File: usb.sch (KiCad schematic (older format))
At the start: 27 parts, among them IC1 EP4CE10F17, P1 USB_A, U23 FT313HL-LQFP64-0.5, U25 TPS2024D, Y2 Geyer_KX7_12MHz

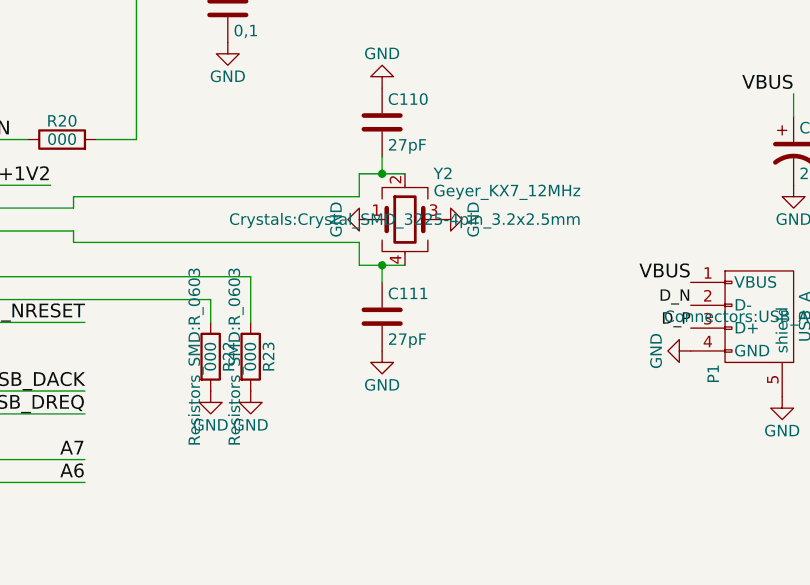
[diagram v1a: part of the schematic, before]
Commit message: Crystals fix, USB rearranged
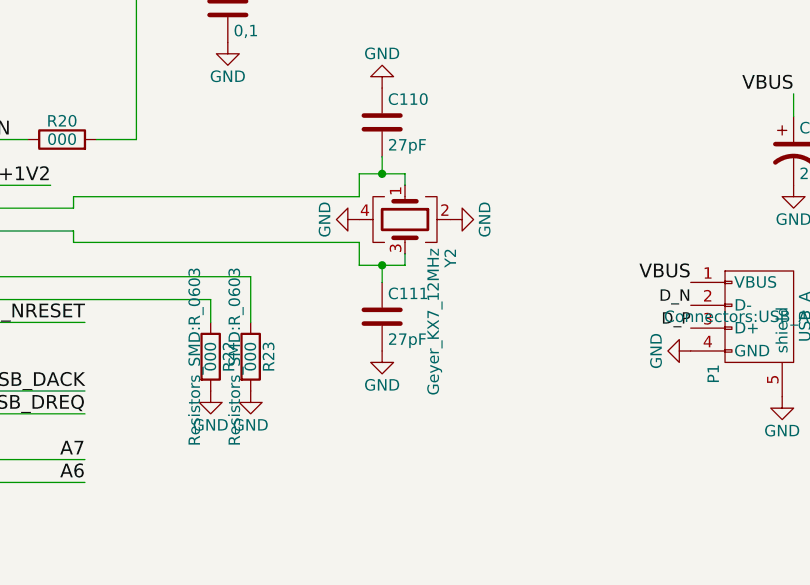
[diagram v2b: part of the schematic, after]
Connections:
- net GND: now also Y2.2, Y2.4; no longer Y2.1, Y2.3
- net at C111.1, U23.44 (X1/CLKIN): now also Y2.3; no longer Y2.4
- net at C110.2, U23.45 (X2): now also Y2.1; no longer Y2.2
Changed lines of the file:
@@
 F 0 "Y2" H 9075 3475 50  0000 L CNN
 F 1 "Geyer_KX7_12MHz" H 9075 3400 50  0000 L CNN
-F 2 "Crystals:Crystal_SMD_3225-4pin_3.2x2.5mm" H 8950 3275 50  0000 C CNN
+F 2 "Crystals:Crystal_SMD_3225-4pin_3.2x2.5mm" H 8950 3275 50  0001 C CNN
 F 3 "" H 8950 3275 50  0000 C CNN
 	1    8950 3275
-	1    0    0    -1
+	0    1    1    0
 $EndComp
 Wire Wire Line
@@
 L GND #PWR0164
 U 1 1 5891C617
-P 8800 3275
-F 0 "#PWR0164" H 8800 3025 50  0001 C CNN
-F 1 "GND" H 8800 3125 50  0000 C CNN
-F 2 "" H 8800 3275 50  0000 C CNN
-F 3 "" H 8800 3275 50  0000 C CNN
-	1    8800 3275
+P 8750 3275
+F 0 "#PWR0164" H 8750 3025 50  0001 C CNN
+F 1 "GND" H 8750 3125 50  0000 C CNN
+F 2 "" H 8750 3275 50  0000 C CNN
+F 3 "" H 8750 3275 50  0000 C CNN
+	1    8750 3275
 	0    1    1    0
 $EndComp
@@
 L GND #PWR0165
 U 1 1 5891C65E
-P 9100 3275
-F 0 "#PWR0165" H 9100 3025 50  0001 C CNN
-F 1 "GND" H 9100 3125 50  0000 C CNN
-F 2 "" H 9100 3275 50  0000 C CNN
-F 3 "" H 9100 3275 50  0000 C CNN
-	1    9100 3275
+P 9150 3275
+F 0 "#PWR0165" H 9150 3025 50  0001 C CNN
+F 1 "GND" H 9150 3125 50  0000 C CNN
+F 2 "" H 9150 3275 50  0000 C CNN
+F 3 "" H 9150 3275 50  0000 C CNN
+	1    9150 3275
 	0    -1   -1   0
 $EndComp
@@
 Text GLabel 5125 5100 3    39   Input ~ 0
 ETHSD15
+Wire Wire Line
+	8950 3075 8950 3125
+Wire Wire Line
+	8950 3475 8950 3425
 $EndSCHEMATC

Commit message: Added VBUS and OC LEDs
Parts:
- added D1: RED, LEDs:LED_0603, symbol LED_Small_ALT
- added D2: GREEN, LEDs:LED_0603, symbol LED_Small_ALT
- added R26, R27: TBD, Resistors_SMD:R_0603, symbol R
- Y2: value Geyer_KX7_12MHz -> 12MHz
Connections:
- net +3V3: now also R26.1
- net GND: now also R27.2
- net VBUS: now also D2.2 (A)
- net at R24.2, R25.1, U25.5 (~OC): now also D1.1 (K)
- new net: D2.1 (K), R27.1
- new net: D1.2 (A), R26.2
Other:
- moved on the sheet: C108, C109, C65, C66, C67, C68, C69, C70, R25

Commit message: Add CPEx config resistors
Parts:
- added R28, R29: 000, Resistors_SMD:R_0603, symbol R
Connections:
- net CPE0: now also R28.2
- net CPE1: now also R29.2
- net GND: now also R28.1, R29.1
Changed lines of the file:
@@
 $EndComp
 $Comp
-L GND #PWR151
+L GND #PWR153
 U 1 1 587F942A
 P 7000 3425
-F 0 "#PWR151" H 7000 3175 50  0001 C CNN
+F 0 "#PWR153" H 7000 3175 50  0001 C CNN
 F 1 "GND" H 7000 3275 50  0000 C CNN
 F 2 "" H 7000 3425 50  0000 C CNN
@@
 $EndComp
 $Comp
-L GND #PWR150
+L GND #PWR152
 U 1 1 587F944F
 P 7000 3025
-F 0 "#PWR150" H 7000 2775 50  0001 C CNN
+F 0 "#PWR152" H 7000 2775 50  0001 C CNN
 F 1 "GND" H 7000 2875 50  0000 C CNN
 F 2 "" H 7000 3025 50  0000 C CNN
@@
 $EndComp
 $Comp
-L GND #PWR147
+L GND #PWR149
 U 1 1 587F9489
 P 5825 2450
-F 0 "#PWR147" H 5825 2200 50  0001 C CNN
+F 0 "#PWR149" H 5825 2200 50  0001 C CNN
 F 1 "GND" H 5825 2300 50  0000 C CNN
 F 2 "" H 5825 2450 50  0000 C CNN
@@
 $EndComp
 $Comp
-L GND #PWR144
+L GND #PWR146
 U 1 1 587F9497
 P 5425 2450
-F 0 "#PWR144" H 5425 2200 50  0001 C CNN
+F 0 "#PWR146" H 5425 2200 50  0001 C CNN
 F 1 "GND" H 5425 2300 50  0000 C CNN
 F 2 "" H 5425 2450 50  0000 C CNN
@@
 $EndComp
 $Comp
-L +3V3 #PWR165
+L +3V3 #PWR167
 U 1 1 587FA4A0
 P 10075 675
-F 0 "#PWR165" H 10175 725 20  0001 C CNN
+F 0 "#PWR167" H 10175 725 20  0001 C CNN
 F 1 "+3V3" H 10075 765 30  0000 C CNN
 F 2 "" H 10075 675 60  0000 C CNN
@@
 $EndComp
 $Comp
-L GND #PWR166
+L GND #PWR168
 U 1 1 587FA6CC
 P 10075 1075
-F 0 "#PWR166" H 10075 825 50  0001 C CNN
+F 0 "#PWR168" H 10075 825 50  0001 C CNN
 F 1 "GND" H 10075 925 50  0000 C CNN
 F 2 "" H 10075 1075 50  0000 C CNN
@@
 $EndComp
 $Comp
-L +3V3 #PWR146
+L +3V3 #PWR148
 U 1 1 587FB177
 P 5725 5100
-F 0 "#PWR146" H 5825 5150 20  0001 C CNN
+F 0 "#PWR148" H 5825 5150 20  0001 C CNN
 F 1 "+3V3" H 5725 5190 30  0000 C CNN
 F 2 "" H 5725 5100 60  0000 C CNN
@@
 $EndComp
 $Comp
-L +3V3 #PWR152
+L +3V3 #PWR154
 U 1 1 587FB222
 P 7000 4225
-F 0 "#PWR152" H 7100 4275 20  0001 C CNN
+F 0 "#PWR154" H 7100 4275 20  0001 C CNN
 F 1 "+3V3" H 7000 4315 30  0000 C CNN
 F 2 "" H 7000 4225 60  0000 C CNN
@@
 +1V2
 $Comp
-L +3V3 #PWR145
+L +3V3 #PWR147
 U 1 1 587FFC16
 P 5625 2450
-F 0 "#PWR145" H 5725 2500 20  0001 C CNN
+F 0 "#PWR147" H 5725 2500 20  0001 C CNN
 F 1 "+3V3" H 5625 2540 30  0000 C CNN
 F 2 "" H 5625 2450 60  0000 C CNN
@@
 $EndComp
 $Comp
-L GND #PWR149
+L GND #PWR151
 U 1 1 588FBF68
 P 6750 2450
-F 0 "#PWR149" H 6750 2200 50  0001 C CNN
+F 0 "#PWR151" H 6750 2200 50  0001 C CNN
 F 1 "GND" H 6750 2300 50  0000 C CNN
 F 2 "" H 6750 2450 50  0000 C CNN
@@
 D_P
 $Comp
-L GND #PWR168
+L GND #PWR170
 U 1 1 588FD418
 P 10200 3850
-F 0 "#PWR168" H 10200 3600 50  0001 C CNN
+F 0 "#PWR170" H 10200 3600 50  0001 C CNN
 F 1 "GND" H 10200 3700 50  0000 C CNN
 F 2 "" H 10200 3850 50  0000 C CNN
@@
 $EndComp
 $Comp
-L GND #PWR170
+L GND #PWR172
 U 1 1 588FDBE9
 P 10600 4050
-F 0 "#PWR170" H 10600 3800 50  0001 C CNN
+F 0 "#PWR172" H 10600 3800 50  0001 C CNN
 F 1 "GND" H 10600 3900 50  0000 C CNN
 F 2 "" H 10600 4050 50  0000 C CNN
@@
 $EndComp
 $Comp
-L GND #PWR158
+L GND #PWR160
 U 1 1 5890EDC6
 P 8700 1825
-F 0 "#PWR158" H 8700 1575 50  0001 C CNN
+F 0 "#PWR160" H 8700 1575 50  0001 C CNN
 F 1 "GND" H 8700 1675 50  0000 C CNN
 F 2 "" H 8700 1825 50  0000 C CNN
@@
 $EndComp
 $Comp
-L GND #PWR157
+L GND #PWR159
 U 1 1 5890F077
 P 8350 2500
-F 0 "#PWR157" H 8350 2250 50  0001 C CNN
+F 0 "#PWR159" H 8350 2250 50  0001 C CNN
 F 1 "GND" H 8350 2350 50  0000 C CNN
 F 2 "" H 8350 2500 50  0000 C CNN
@@
 $EndComp
 $Comp
-L +3V3 #PWR153
+L +3V3 #PWR155
 U 1 1 589100DF
 P 7775 1625
-F 0 "#PWR153" H 7875 1675 20  0001 C CNN
+F 0 "#PWR155" H 7875 1675 20  0001 C CNN
 F 1 "+3V3" H 7775 1715 30  0000 C CNN
 F 2 "" H 7775 1625 60  0000 C CNN
@@
 $EndComp
 $Comp
-L +5VDC #PWR156
+L +5VDC #PWR158
 U 1 1 58911317
 P 8350 1550
-F 0 "#PWR156" H 8450 1600 20  0001 C CNN
+F 0 "#PWR158" H 8450 1600 20  0001 C CNN
 F 1 "+5VDC" H 8350 1640 30  0000 C CNN
 F 2 "" H 8350 1550 60  0000 C CNN
@@
 	10600 2125 10750 2125
 Wire Wire Line
-	4925 2450 4925 2200
-Wire Wire Line
-	5125 2450 5125 2200
+	4925 2125 4925 2450
+Wire Wire Line
+	5125 1950 5125 2450
 Text Label 5125 2200 3    60   ~ 0
 CPE0
@@
 	8100 3625 7000 3625
 $Comp
-L GND #PWR154
+L GND #PWR156
 U 1 1 58918521
 P 8100 4025
-F 0 "#PWR154" H 8100 3775 50  0001 C CNN
+F 0 "#PWR156" H 8100 3775 50  0001 C CNN
 F 1 "GND" H 8100 3875 50  0000 C CNN
 F 2 "" H 8100 4025 50  0000 C CNN
@@
 $EndComp
 $Comp
-L GND #PWR155
+L GND #PWR157
 U 1 1 58918565
 P 8275 4025
-F 0 "#PWR155" H 8275 3775 50  0001 C CNN
+F 0 "#PWR157" H 8275 3775 50  0001 C CNN
 F 1 "GND" H 8275 3875 50  0000 C CNN
 F 2 "" H 8275 4025 50  0000 C CNN
@@
 $EndComp
 $Comp
-L +3V3 #PWR164
+L +3V3 #PWR166
 U 1 1 58919A0E
 P 9800 1550
-F 0 "#PWR164" H 9900 1600 20  0001 C CNN
+F 0 "#PWR166" H 9900 1600 20  0001 C CNN
 F 1 "+3V3" H 9800 1640 30  0000 C CNN
 F 2 "" H 9800 1550 60  0000 C CNN
@@
 $EndComp
 $Comp
-L GND #PWR163
+L GND #PWR165
 U 1 1 5891AE93
 P 9575 2625
-F 0 "#PWR163" H 9575 2375 50  0001 C CNN
+F 0 "#PWR165" H 9575 2375 50  0001 C CNN
 F 1 "GND" H 9575 2475 50  0000 C CNN
 F 2 "" H 9575 2625 50  0000 C CNN
@@
 $EndComp
 $Comp
-L GND #PWR159
+L GND #PWR161
 U 1 1 5891C617
 P 8750 3275
-F 0 "#PWR159" H 8750 3025 50  0001 C CNN
+F 0 "#PWR161" H 8750 3025 50  0001 C CNN
 F 1 "GND" H 8750 3125 50  0000 C CNN
 F 2 "" H 8750 3275 50  0000 C CNN
@@
 $EndComp
 $Comp
-L GND #PWR162
+L GND #PWR164
 U 1 1 5891C65E
 P 9150 3275
-F 0 "#PWR162" H 9150 3025 50  0001 C CNN
+F 0 "#PWR164" H 9150 3025 50  0001 C CNN
 F 1 "GND" H 9150 3125 50  0000 C CNN
 F 2 "" H 9150 3275 50  0000 C CNN
@@
 Connection ~ 8850 3075
 $Comp
-L GND #PWR161
+L GND #PWR163
 U 1 1 5891DDB7
 P 8850 3850
-F 0 "#PWR161" H 8850 3600 50  0001 C CNN
+F 0 "#PWR163" H 8850 3600 50  0001 C CNN
 F 1 "GND" H 8850 3700 50  0000 C CNN
 F 2 "" H 8850 3850 50  0000 C CNN
@@
 $EndComp
 $Comp
-L GND #PWR160
+L GND #PWR162
 U 1 1 5891DE04
 P 8850 2700
-F 0 "#PWR160" H 8850 2450 50  0001 C CNN
+F 0 "#PWR162" H 8850 2450 50  0001 C CNN
 F 1 "GND" H 8850 2550 50  0000 C CNN
 F 2 "" H 8850 2700 50  0000 C CNN
@@
 Connection ~ 6875 1225
 $Comp
-L GND #PWR148
+L GND #PWR150
 U 1 1 58A7680E
 P 6625 1225
-F 0 "#PWR148" H 6625 975 50  0001 C CNN
+F 0 "#PWR150" H 6625 975 50  0001 C CNN
 F 1 "GND" H 6625 1075 50  0000 C CNN
 F 2 "" H 6625 1225 50  0000 C CNN
@@
 $EndComp
 $Comp
-L GND #PWR169
+L GND #PWR171
 U 1 1 5895CD67
 P 10275 4925
-F 0 "#PWR169" H 10275 4675 50  0001 C CNN
+F 0 "#PWR171" H 10275 4675 50  0001 C CNN
 F 1 "GND" H 10275 4775 50  0000 C CNN
 F 2 "" H 10275 4925 50  0000 C CNN
@@
 $EndComp
 $Comp
-L +3V3 #PWR167
+L +3V3 #PWR169
 U 1 1 5895DF10
 P 10125 1550
-F 0 "#PWR167" H 10225 1600 20  0001 C CNN
+F 0 "#PWR169" H 10225 1600 20  0001 C CNN
 F 1 "+3V3" H 10125 1640 30  0000 C CNN
 F 2 "" H 10125 1550 60  0000 C CNN
@@
 	1    0    0    -1
 $EndComp
+$Comp
+L R R29
+U 1 1 5897A724
+P 4550 2125
+F 0 "R29" V 4630 2125 50  0000 C CNN
+F 1 "000" V 4550 2125 50  0000 C CNN
+F 2 "Resistors_SMD:R_0603" V 4480 2125 50  0001 C CNN
+F 3 "" H 4550 2125 50  0000 C CNN
+	1    4550 2125
+	0    -1   -1   0
+$EndComp
+$Comp
+L R R28
+U 1 1 5897A842
+P 4550 1950
+F 0 "R28" V 4630 1950 50  0000 C CNN
+F 1 "000" V 4550 1950 50  0000 C CNN
+F 2 "Resistors_SMD:R_0603" V 4480 1950 50  0001 C CNN
+F 3 "" H 4550 1950 50  0000 C CNN
+	1    4550 1950
+	0    -1   -1   0
+$EndComp
+$Comp
+L GND #PWR144
+U 1 1 5897A8C7
+P 4400 1950
+F 0 "#PWR144" H 4400 1700 50  0001 C CNN
+F 1 "GND" H 4400 1800 50  0000 C CNN
+F 2 "" H 4400 1950 50  0000 C CNN
+F 3 "" H 4400 1950 50  0000 C CNN
+	1    4400 1950
+	0    1    1    0
+$EndComp
+$Comp
+L GND #PWR145
+U 1 1 5897A935
+P 4400 2125
+F 0 "#PWR145" H 4400 1875 50  0001 C CNN
+F 1 "GND" H 4400 1975 50  0000 C CNN
+F 2 "" H 4400 2125 50  0000 C CNN
+F 3 "" H 4400 2125 50  0000 C CNN
+	1    4400 2125
+	0    1    1    0
+$EndComp
+Wire Wire Line
+	4700 1950 5125 1950
+Wire Wire Line
+	4925 2125 4700 2125
 $EndSCHEMATC
